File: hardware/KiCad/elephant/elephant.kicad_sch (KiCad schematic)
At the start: 33 parts, among them J1 Conn_01x05_Pin, J2 Conn_01x04_Pin, SW1 SW_TILT, U1 SSM2518, U2 STM32F401CCUx, U4 M95M04, Y1 32.768kHz, 6pF, 50kΩ, Y2 25MHz, 9pF

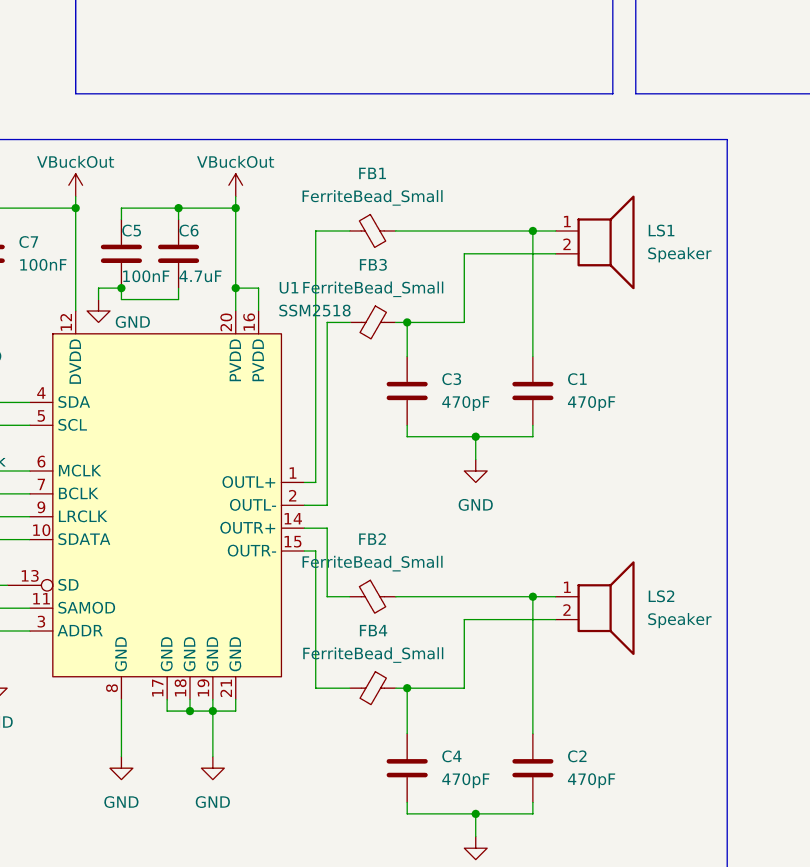
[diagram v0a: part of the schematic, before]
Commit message: Planning ahead for evaluation board.
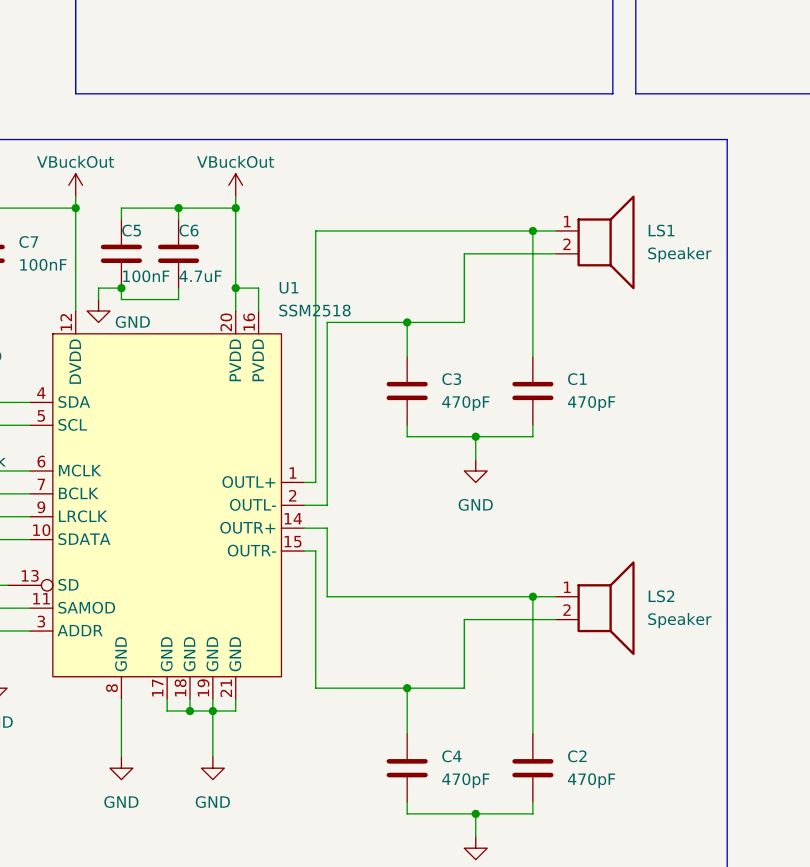
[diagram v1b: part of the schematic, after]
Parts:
- removed FB1, FB2, FB3, FB4: FerriteBead_Small, Inductor_SMD:L_0402_1005Metric, symbol Device:FerriteBead_Small
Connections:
- net at C1.1, LS1.1: now also U1.1 (OUTL+)
- net at C4.1, LS2.2: now also U1.15 (OUTR-)
- net at C3.1, LS1.2: now also U1.2 (OUTL-)
- net at U1.14 (OUTR+): now also C2.1, LS2.1

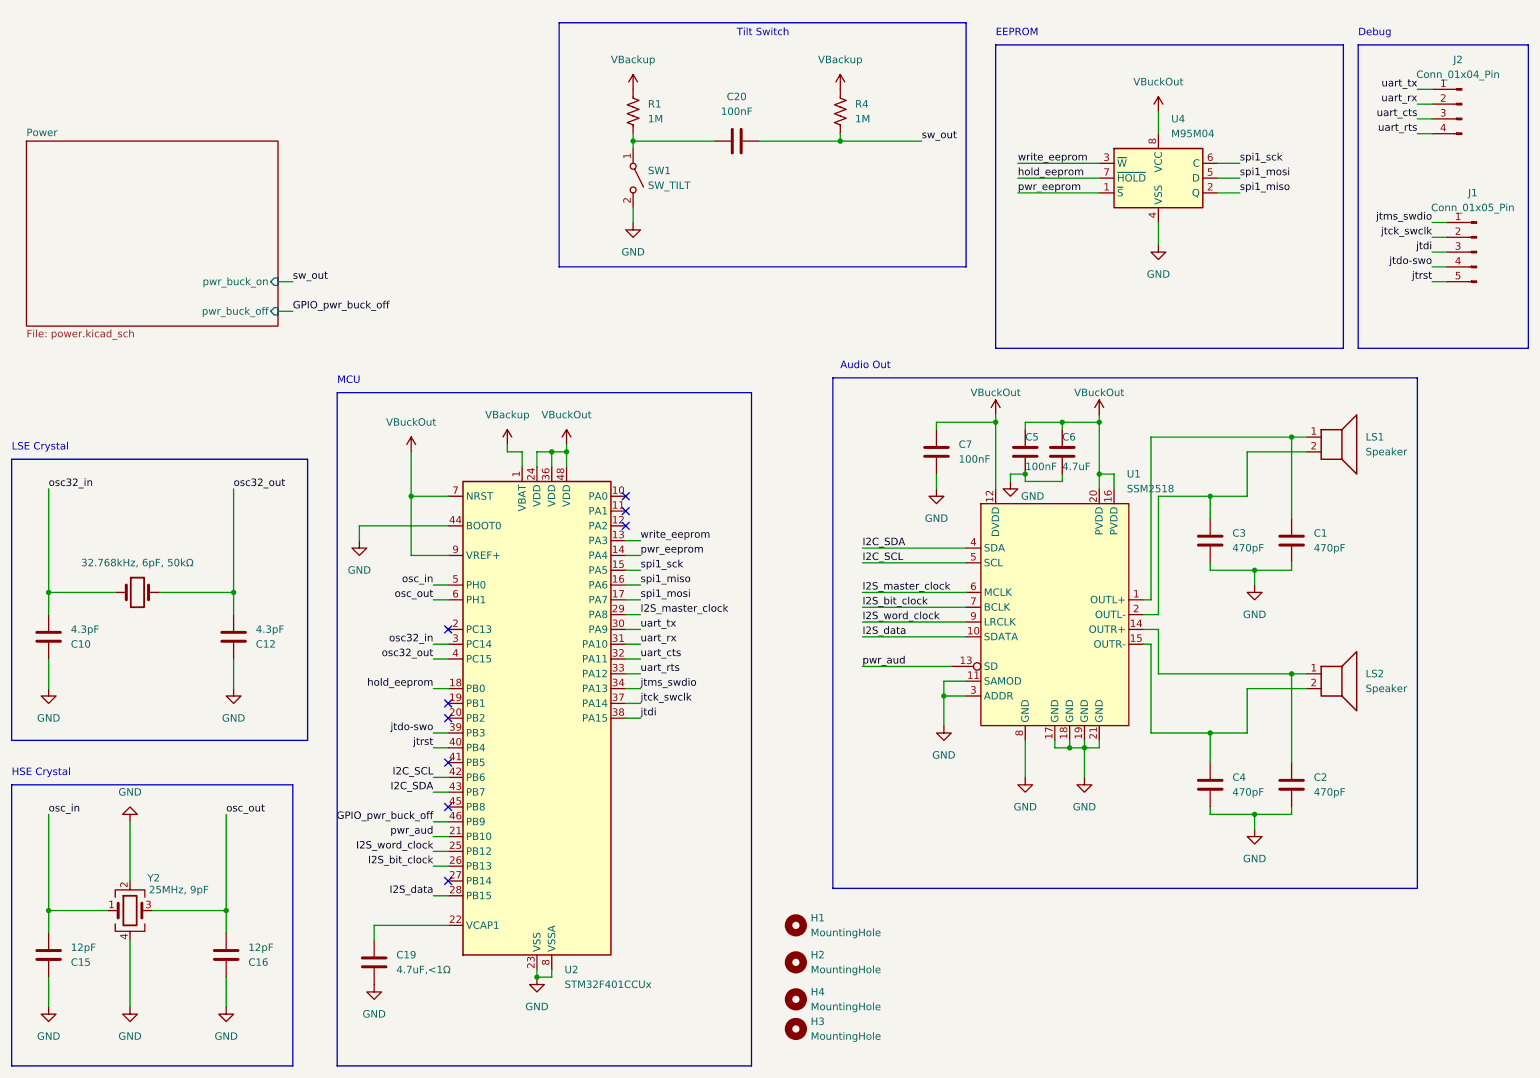
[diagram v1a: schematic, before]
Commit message: Tilt switch tests completed; tilt switch circuit verified.
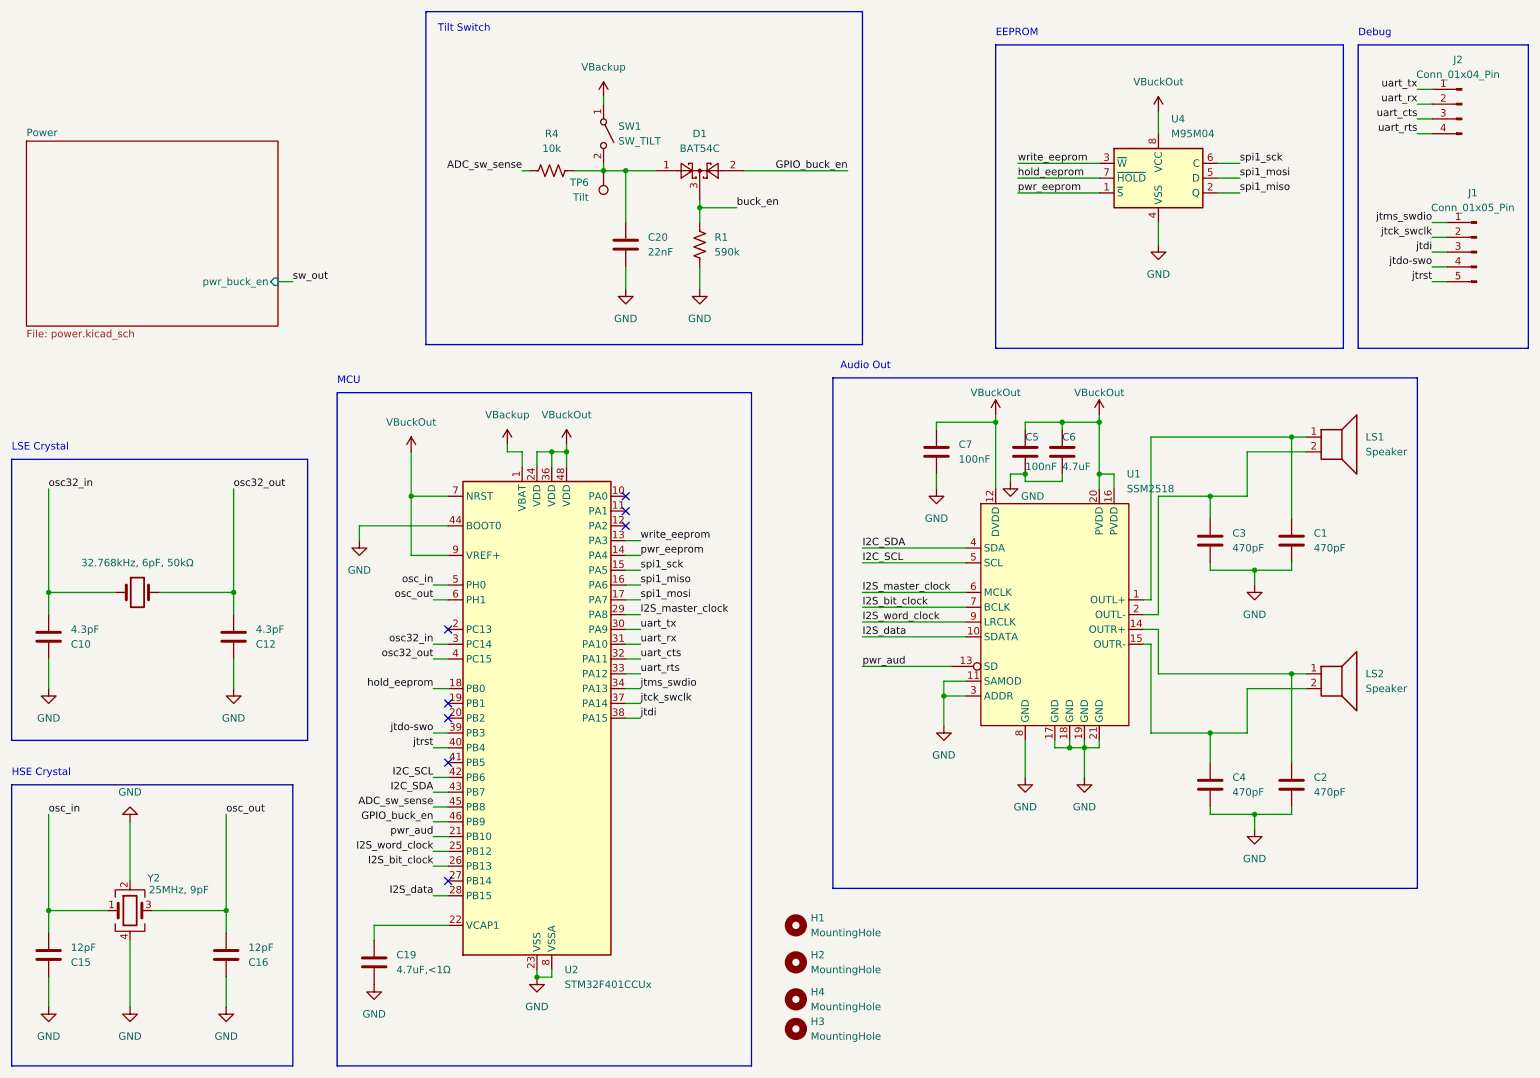
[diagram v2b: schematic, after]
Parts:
- added D1: BAT54C, Package_TO_SOT_SMD:SOT-23, symbol Diode:BAT54C
- added TP6: Tilt, TestPoint:TestPoint_Pad_D1.0mm, symbol Connector:TestPoint
- C20: value 100nF -> 22nF; footprint Capacitor_SMD:C_0603_1608Metric -> Capacitor_SMD:C_0805_2012Metric
- R1: value 1M -> 590k; footprint Resistor_SMD:R_0603_1608Metric -> Resistor_SMD:R_0805_2012Metric
- R4: value 1M -> 10k
- SW1: footprint Connector_PinHeader_2.54mm:PinHeader_1x02_P2.54mm_Vertical -> Lou:Tilt Switch
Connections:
- net GND: now also C20.2, R1.2; no longer SW1.2 (B)
- net VBackup: now also SW1.1 (A); no longer R1.1, R4.1
- net sw_out: no longer C20.1, R4.2
- net ADC_sw_sense: now reaches U2.45 (PB8)
- net ADC_sw_sense: now also R4.2
- net GPIO_pwr_buck_off renamed GPIO_buck_en
- net GPIO_buck_en: now also D1.2
- new net: C20.1, D1.1, R4.1, SW1.2 (B), TP6.1
- new net buck_en: D1.3, R1.1
- no-connect marks 9 -> 8
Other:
- sheet Power ports: added pwr_buck_en; removed pwr_buck_off, pwr_buck_on
- moved on the sheet: C20, R1, SW1
